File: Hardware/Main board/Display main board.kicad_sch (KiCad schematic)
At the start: 11 parts, among them J1 Board to Board

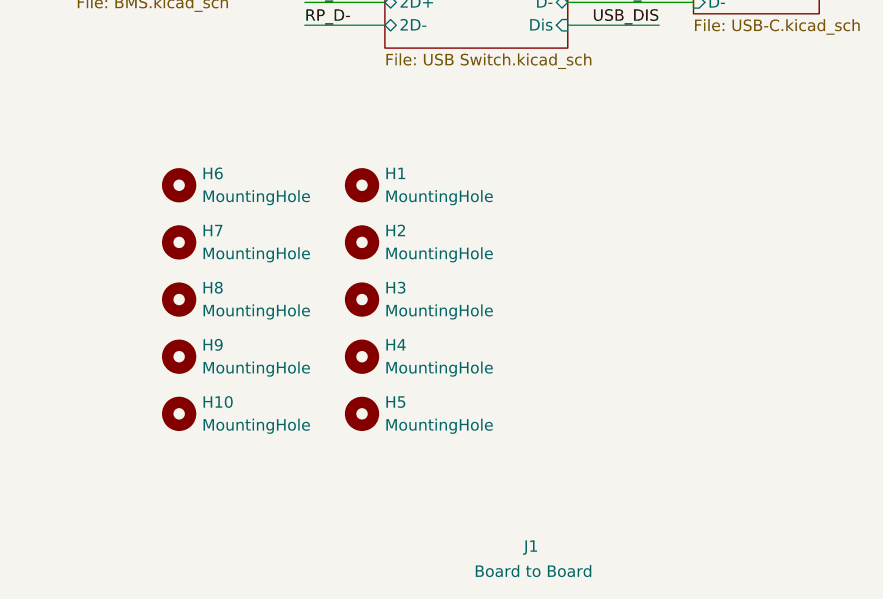
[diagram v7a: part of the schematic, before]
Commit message: Fix BMS_STAT pin
swapped RP2040 footprint for one with thermal vias
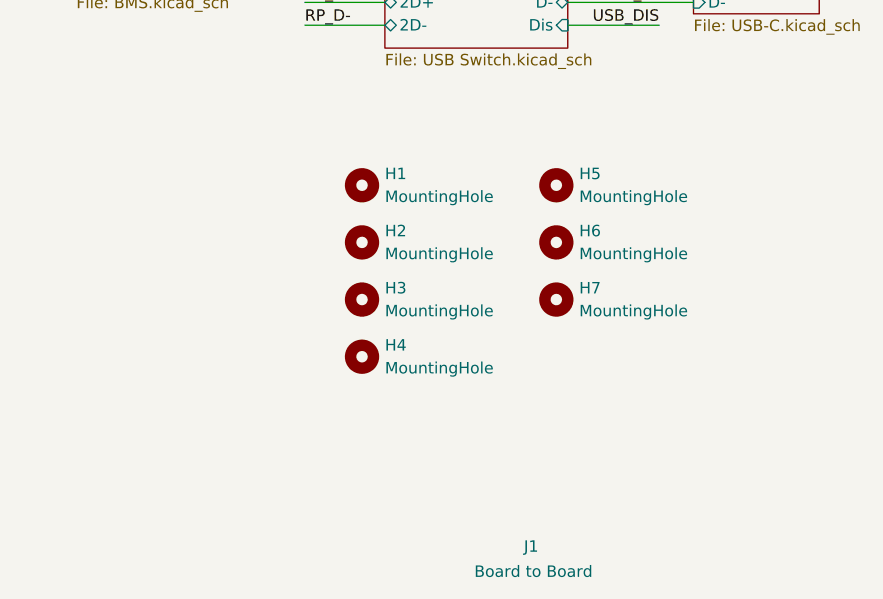
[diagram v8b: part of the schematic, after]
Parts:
- removed H10, H8, H9: MountingHole, symbol Mechanical:MountingHole
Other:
- moved on the sheet: H5, H6, H7
